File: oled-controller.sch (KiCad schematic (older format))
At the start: 2 parts

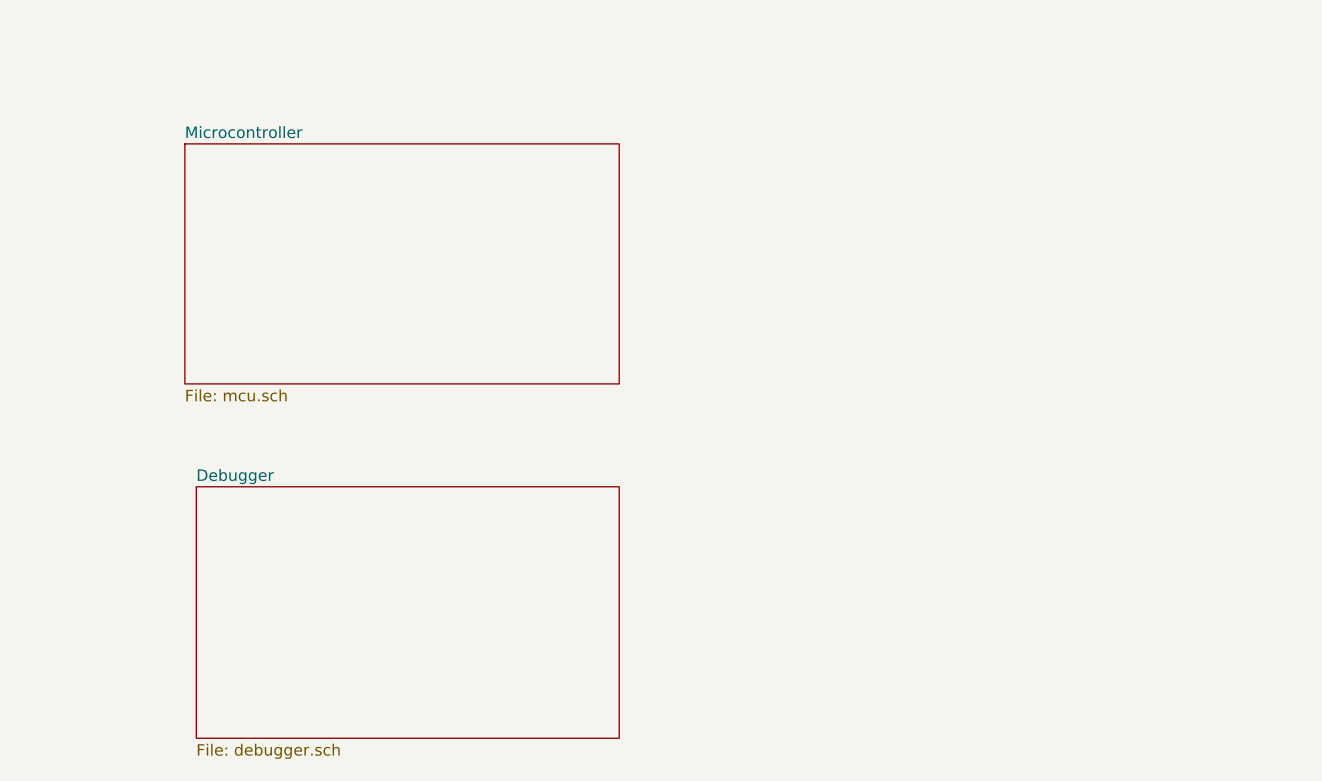
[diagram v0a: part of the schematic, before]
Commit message: Added FT2232D and OLED connector
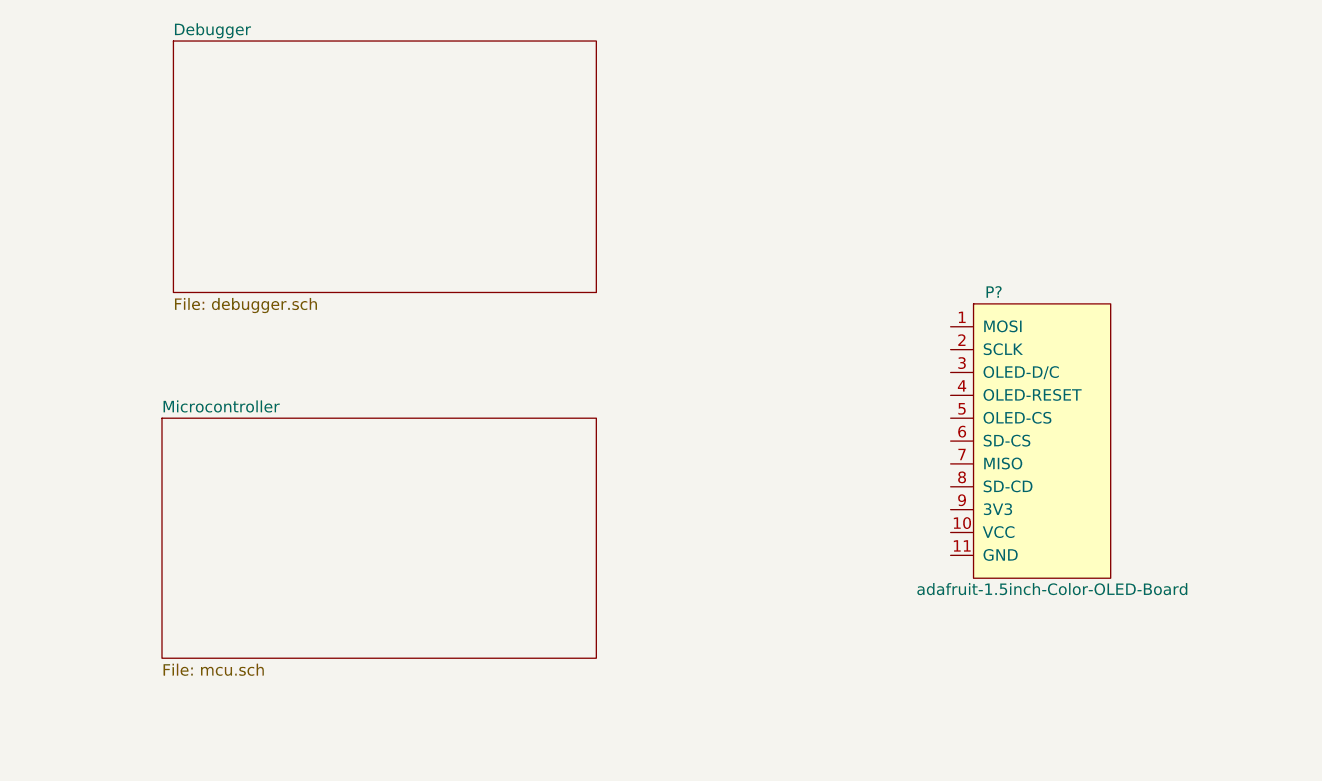
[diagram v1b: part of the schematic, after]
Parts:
- added P?: adafruit-1.5inch-Color-OLED-Board, symbol Matthias:adafruit-1.5inch-Color-OLED-Board
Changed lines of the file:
@@
 EESchema Schematic File Version 4
+LIBS:oled-controller-cache
 EELAYER 26 0
 EELAYER END
@@
 $EndDescr
 $Sheet
-S 5350 2150 1900 1050
+S 5250 3350 1900 1050
 U 5C795DEE
 F0 "Microcontroller" 50
@@
 $EndSheet
 $Sheet
-S 5400 3650 1850 1100
+S 5300 1700 1850 1100
 U 5C795DF5
 F0 "Debugger" 50
@@
 Text Label 2450 3000 0    50   ~ 0
 DM
+$Comp
+L Matthias:adafruit-1.5inch-Color-OLED-Board P?
+U 1 1 5C79A0AF
+P 9100 3450
+F 0 "P?" H 8850 4100 50  0000 L CNN
+F 1 "adafruit-1.5inch-Color-OLED-Board" H 8550 2800 50  0000 L CNN
+F 2 "" H 8900 3500 50  0001 C CNN
+F 3 "" H 8900 3500 50  0001 C CNN
+	1    9100 3450
+	1    0    0    -1
+$EndComp
 $EndSCHEMATC

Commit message: Moved USB and ESD protection to debugger schematic
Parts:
- removed J?: USB_B_Micro, symbol Connector:USB_B_Micro
- removed U?: USBLC6-2SC6, Package_TO_SOT_SMD:SOT-23-6, symbol Power_Protection:USBLC6-2SC6
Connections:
- net labels removed: DM, DP, GND, USB-DM, USB-DP, VBUS
- wire segments 11 -> 0
- no-connect marks 1 -> 0
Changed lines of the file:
@@
 F1 "mcu.sch" 50
 $EndSheet
-$Sheet
-S 5300 1700 1850 1100
-U 5C795DF5
-F0 "Debugger" 50
-F1 "debugger.sch" 50
-$EndSheet
-$Comp
-L Connector:USB_B_Micro J?
-U 1 1 5C79600D
-P 1800 2850
-F 0 "J?" H 1855 3317 50  0000 C CNN
-F 1 "USB_B_Micro" H 1855 3226 50  0000 C CNN
-F 2 "" H 1950 2800 50  0001 C CNN
-F 3 "~" H 1950 2800 50  0001 C CNN
-	1    1800 2850
-	1    0    0    -1
-$EndComp
-$Comp
-L Power_Protection:USBLC6-2SC6 U?
-U 1 1 5C7961A0
-P 3100 2900
-F 0 "U?" H 2850 3300 50  0000 C CNN
-F 1 "USBLC6-2SC6" H 2700 2500 50  0000 C CNN
-F 2 "Package_TO_SOT_SMD:SOT-23-6" H 2350 3300 50  0001 C CNN
-F 3 "http://www2.st.com/resource/en/datasheet/CD00050750.pdf" H 3300 3250 50  0001 C CNN
-	1    3100 2900
-	1    0    0    -1
-$EndComp
-Wire Wire Line
-	2100 2650 2300 2650
-Wire Wire Line
-	2300 2650 2300 2600
-$Comp
-L power:VBUS #PWR?
-U 1 1 5C79662D
-P 2300 2600
-F 0 "#PWR?" H 2300 2450 50  0001 C CNN
-F 1 "VBUS" H 2315 2773 50  0000 C CNN
-F 2 "" H 2300 2600 50  0001 C CNN
-F 3 "" H 2300 2600 50  0001 C CNN
-	1    2300 2600
-	1    0    0    -1
-$EndComp
-$Comp
-L power:VBUS #PWR?
-U 1 1 5C796643
-P 3100 2400
-F 0 "#PWR?" H 3100 2250 50  0001 C CNN
-F 1 "VBUS" H 3115 2573 50  0000 C CNN
-F 2 "" H 3100 2400 50  0001 C CNN
-F 3 "" H 3100 2400 50  0001 C CNN
-	1    3100 2400
-	1    0    0    -1
-$EndComp
-NoConn ~ 1700 3250
-Wire Wire Line
-	1800 3250 1800 3350
-$Comp
-L power:GND #PWR?
-U 1 1 5C7966C6
-P 1800 3350
-F 0 "#PWR?" H 1800 3100 50  0001 C CNN
-F 1 "GND" H 1805 3177 50  0000 C CNN
-F 2 "" H 1800 3350 50  0001 C CNN
-F 3 "" H 1800 3350 50  0001 C CNN
-	1    1800 3350
-	1    0    0    -1
-$EndComp
-$Comp
-L power:GND #PWR?
-U 1 1 5C7966DC
-P 3100 3400
-F 0 "#PWR?" H 3100 3150 50  0001 C CNN
-F 1 "GND" H 3105 3227 50  0000 C CNN
-F 2 "" H 3100 3400 50  0001 C CNN
-F 3 "" H 3100 3400 50  0001 C CNN
-	1    3100 3400
-	1    0    0    -1
-$EndComp
-Wire Wire Line
-	2100 2850 2400 2850
-Wire Wire Line
-	2400 2850 2400 2800
-Wire Wire Line
-	2400 2800 2600 2800
-Wire Wire Line
-	2600 3000 2400 3000
-Wire Wire Line
-	2400 3000 2400 2950
-Wire Wire Line
-	2400 2950 2100 2950
-Wire Wire Line
-	3600 2800 3950 2800
-Wire Wire Line
-	3600 3000 3950 3000
-Text Label 3650 2800 0    50   ~ 0
-USB-DP
-Text Label 3650 3000 0    50   ~ 0
-USB-DM
-Text Label 2450 2800 0    50   ~ 0
-DP
-Text Label 2450 3000 0    50   ~ 0
-DM
 $Comp
 L Matthias:adafruit-1.5inch-Color-OLED-Board P?

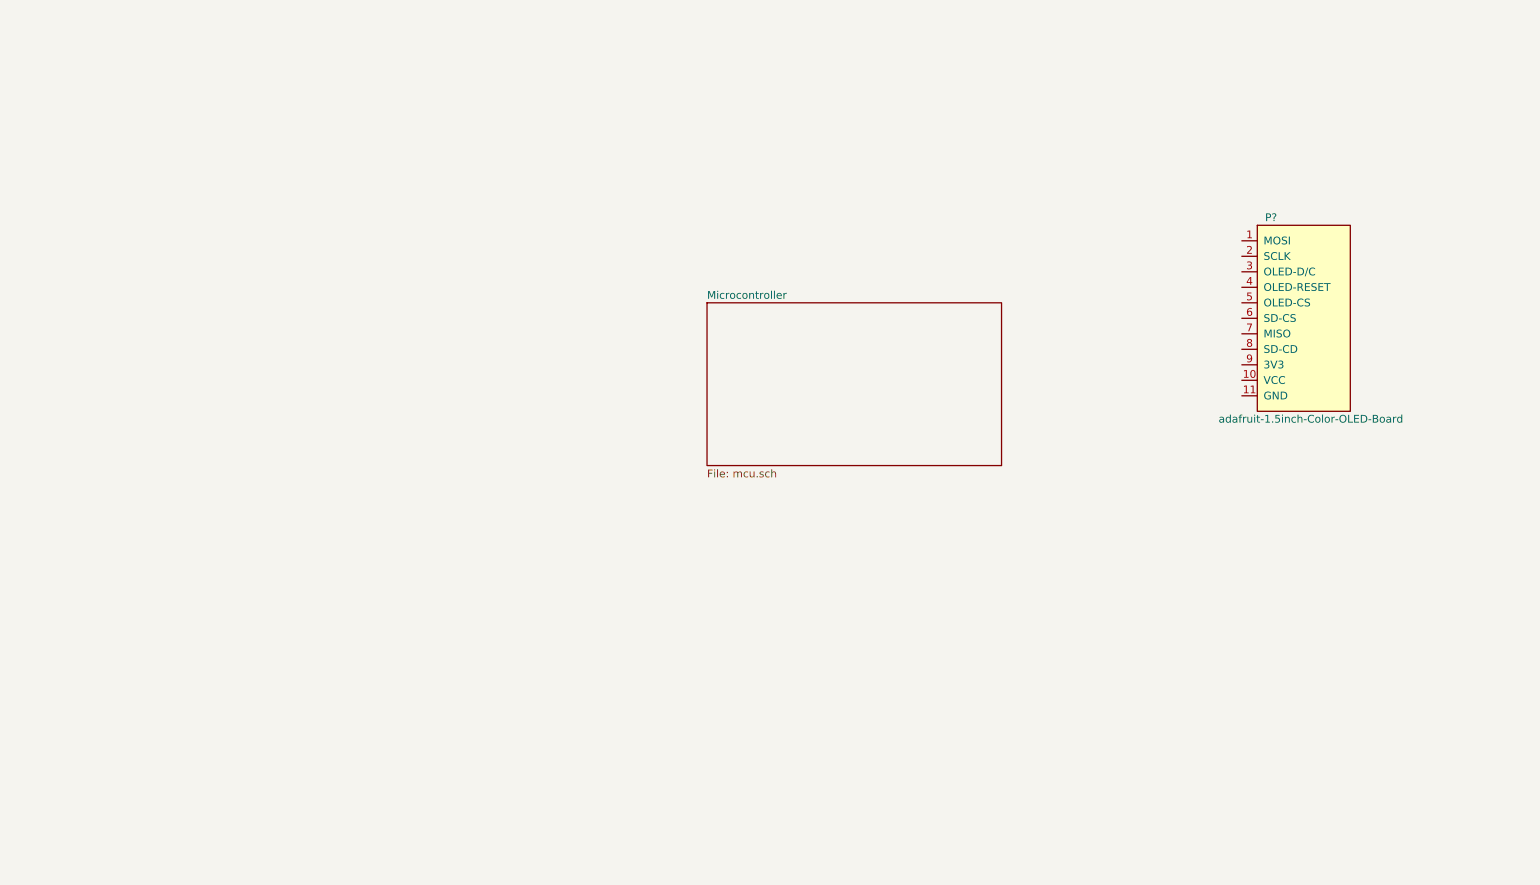
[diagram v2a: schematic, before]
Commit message: Added hierarchical ports for SPI1-3 and others
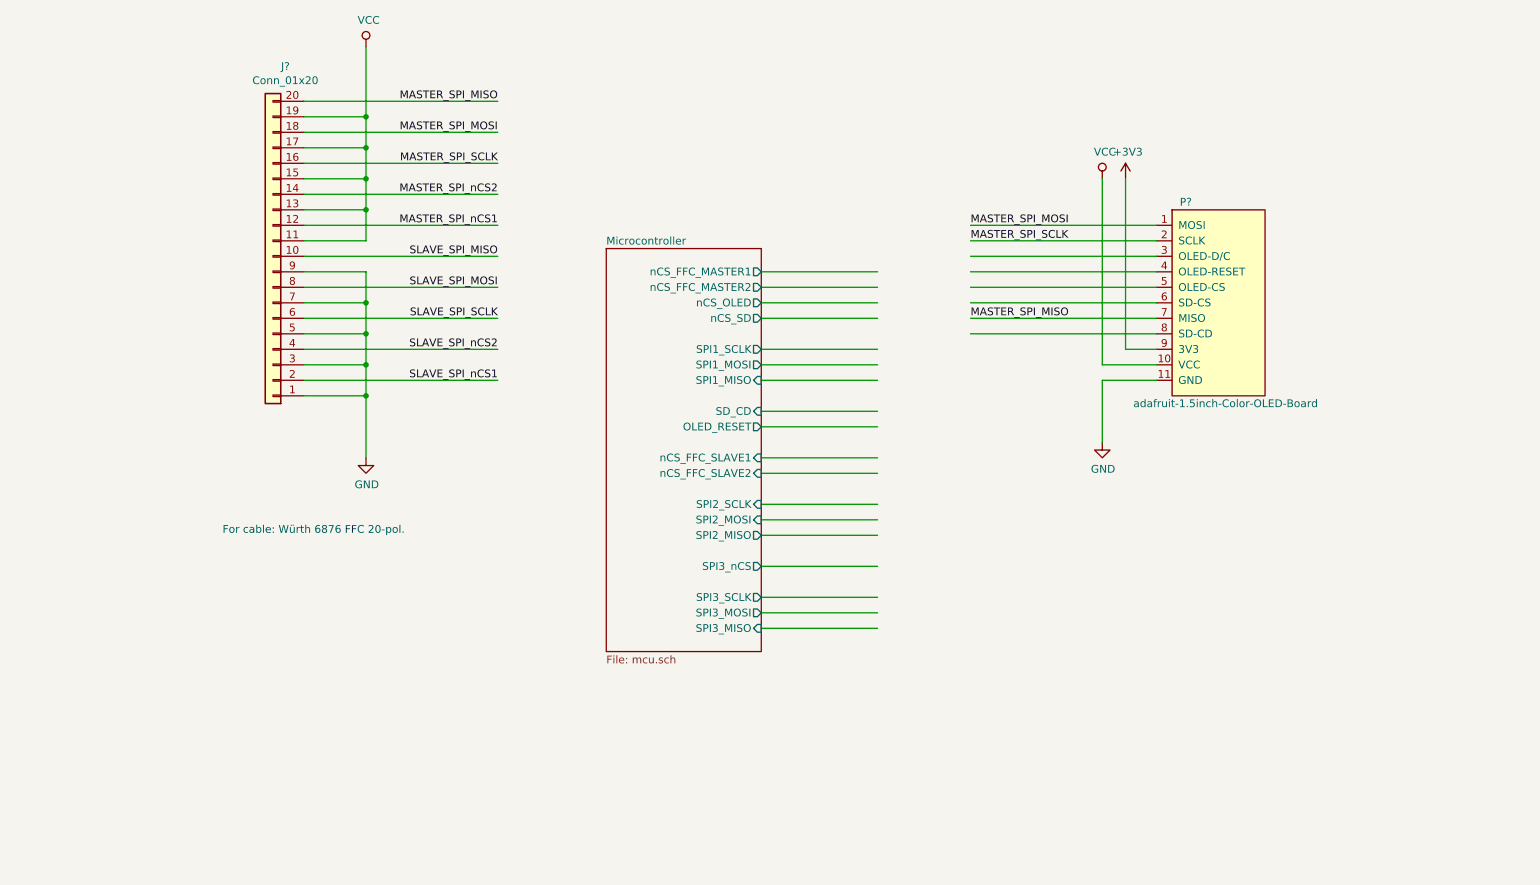
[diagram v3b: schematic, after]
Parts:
- added J?: Conn_01x20, symbol Connector_Generic:Conn_01x20
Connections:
- net labels added: +3V3, GND, MASTER_SPI_MISO, MASTER_SPI_MOSI, MASTER_SPI_SCLK, MASTER_SPI_nCS1, MASTER_SPI_nCS2, SLAVE_SPI_MISO, SLAVE_SPI_MOSI, SLAVE_SPI_SCLK, SLAVE_SPI_nCS1, SLAVE_SPI_nCS2, VCC
- wire segments 0 -> 62
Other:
- note added: "For cable: Würth 6876 FFC 20-pol."
- moved on the sheet: P?

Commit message: Added PMOD connector and bypass capacitors
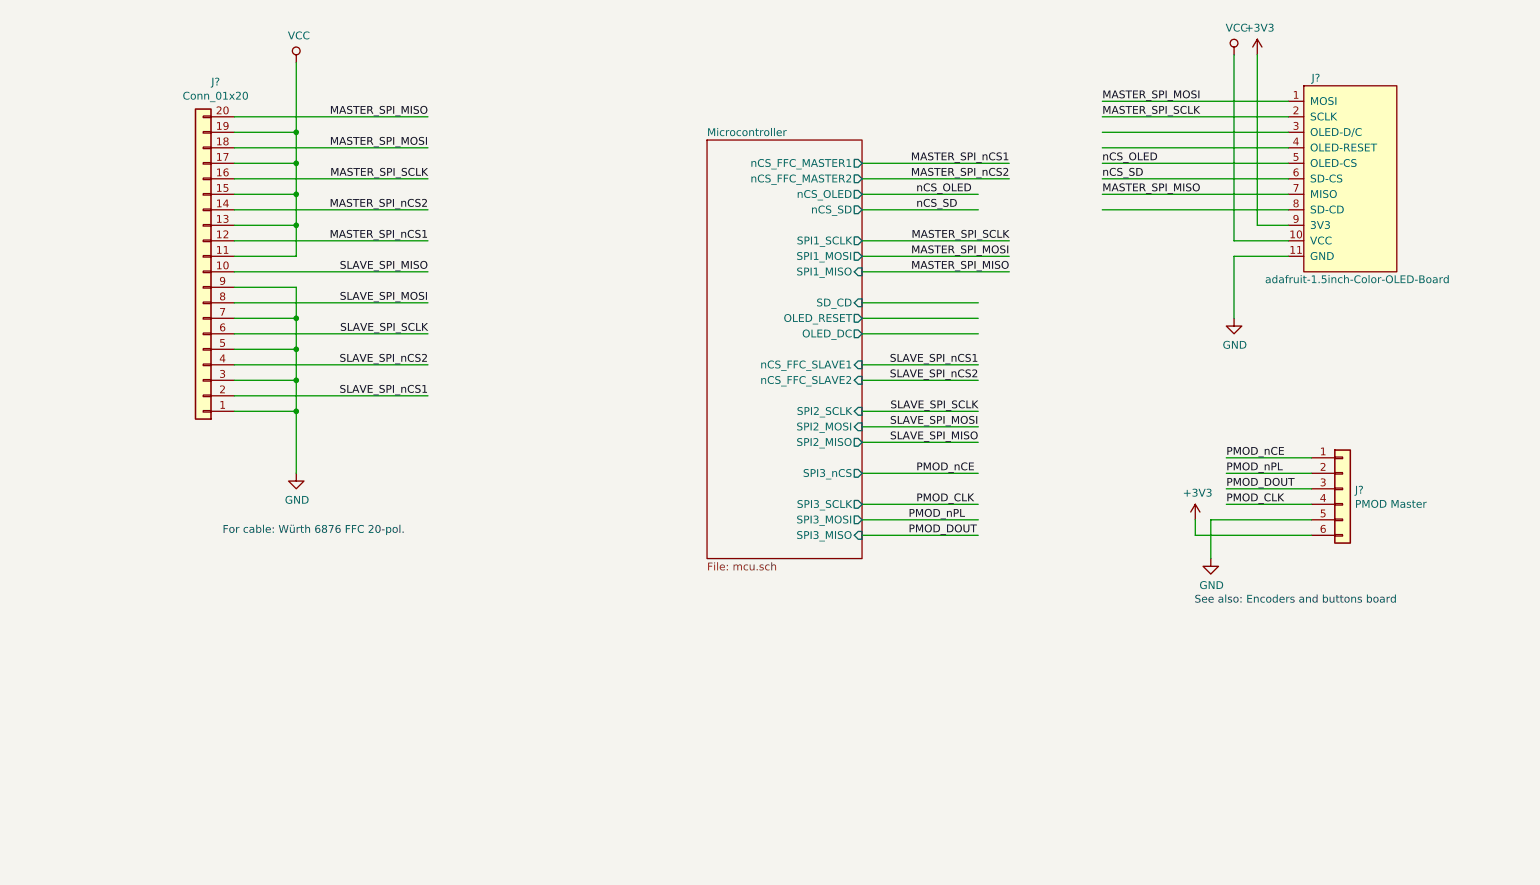
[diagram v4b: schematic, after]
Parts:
- added J?: PMOD Master, Connector_PinHeader_2.54mm:PinHeader_1x06_P2.54mm_Vertical, symbol Connector_Generic:Conn_01x06
- J?: renamed from P?; footprint (none) -> Connector_PinSocket_2.54mm:PinSocket_1x11_P2.54mm_Vertical
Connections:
- net labels added: PMOD_CLK, PMOD_DOUT, PMOD_nCE, PMOD_nPL, nCS_OLED, nCS_SD
- wire segments 62 -> 71
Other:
- note added: "See also: Encoders and buttons board"
- moved on the sheet: J?
